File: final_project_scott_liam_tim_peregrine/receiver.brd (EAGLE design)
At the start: 51.7 x 33 mm, 22 parts

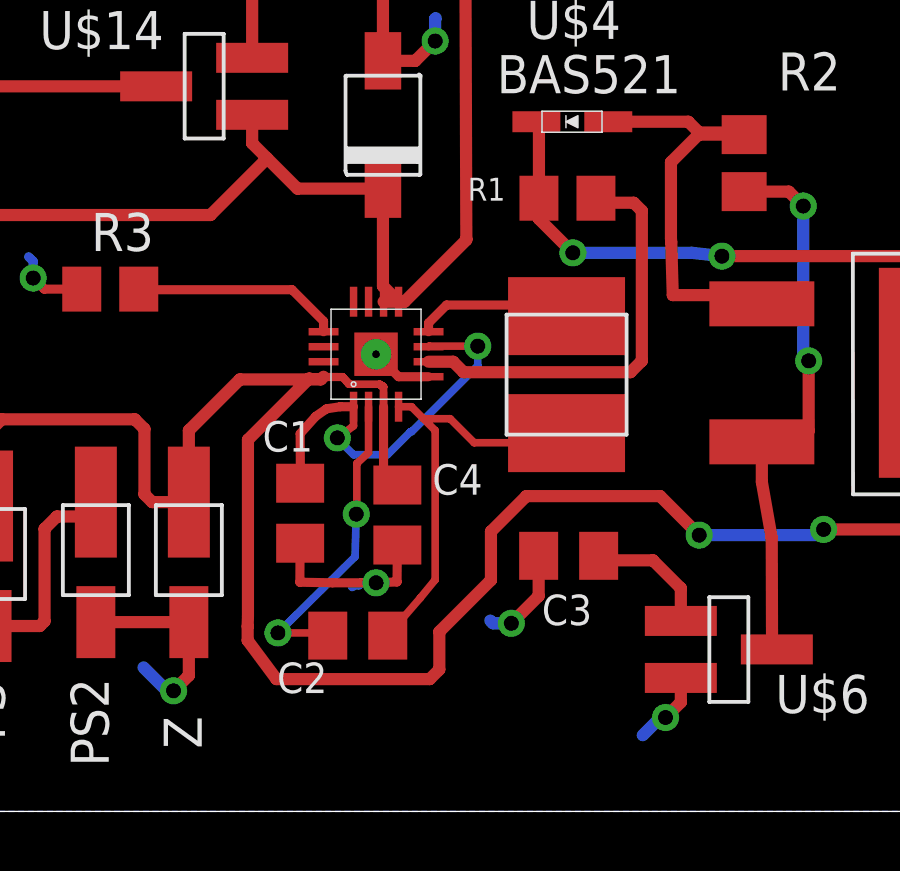
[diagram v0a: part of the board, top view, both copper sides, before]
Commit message: drc checking on receiver
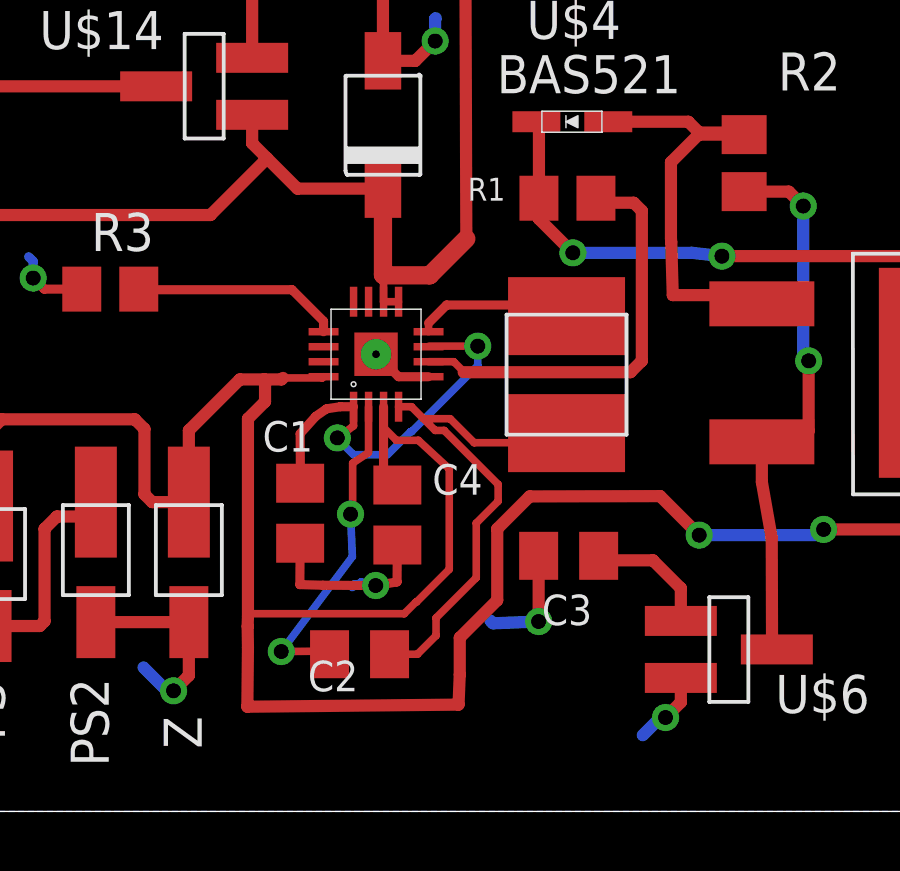
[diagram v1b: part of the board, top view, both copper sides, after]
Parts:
- moved C2 0.62 mm to (23.6, 26.8)
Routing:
- net N$3: track 92.1 -> 104.1 mm
- net N$5: track 14.2 -> 17.3 mm
- net N$4: track 10.7 -> 12.0 mm
- net GND: track 31.0 -> 31.5 mm
